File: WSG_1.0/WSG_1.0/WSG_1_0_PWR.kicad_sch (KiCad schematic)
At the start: 37 parts, among them J2 USB_C_Receptacle_USB2.0_16P, J4 Conn_01x02, U10 TPS22916CYFPR, U11 W25N04KVZEIR, U12 USBLC6-2SC6, U7 BQ25180YBGR, U8 TPS63802DLAR, U9 TPS7A2025PDBVR

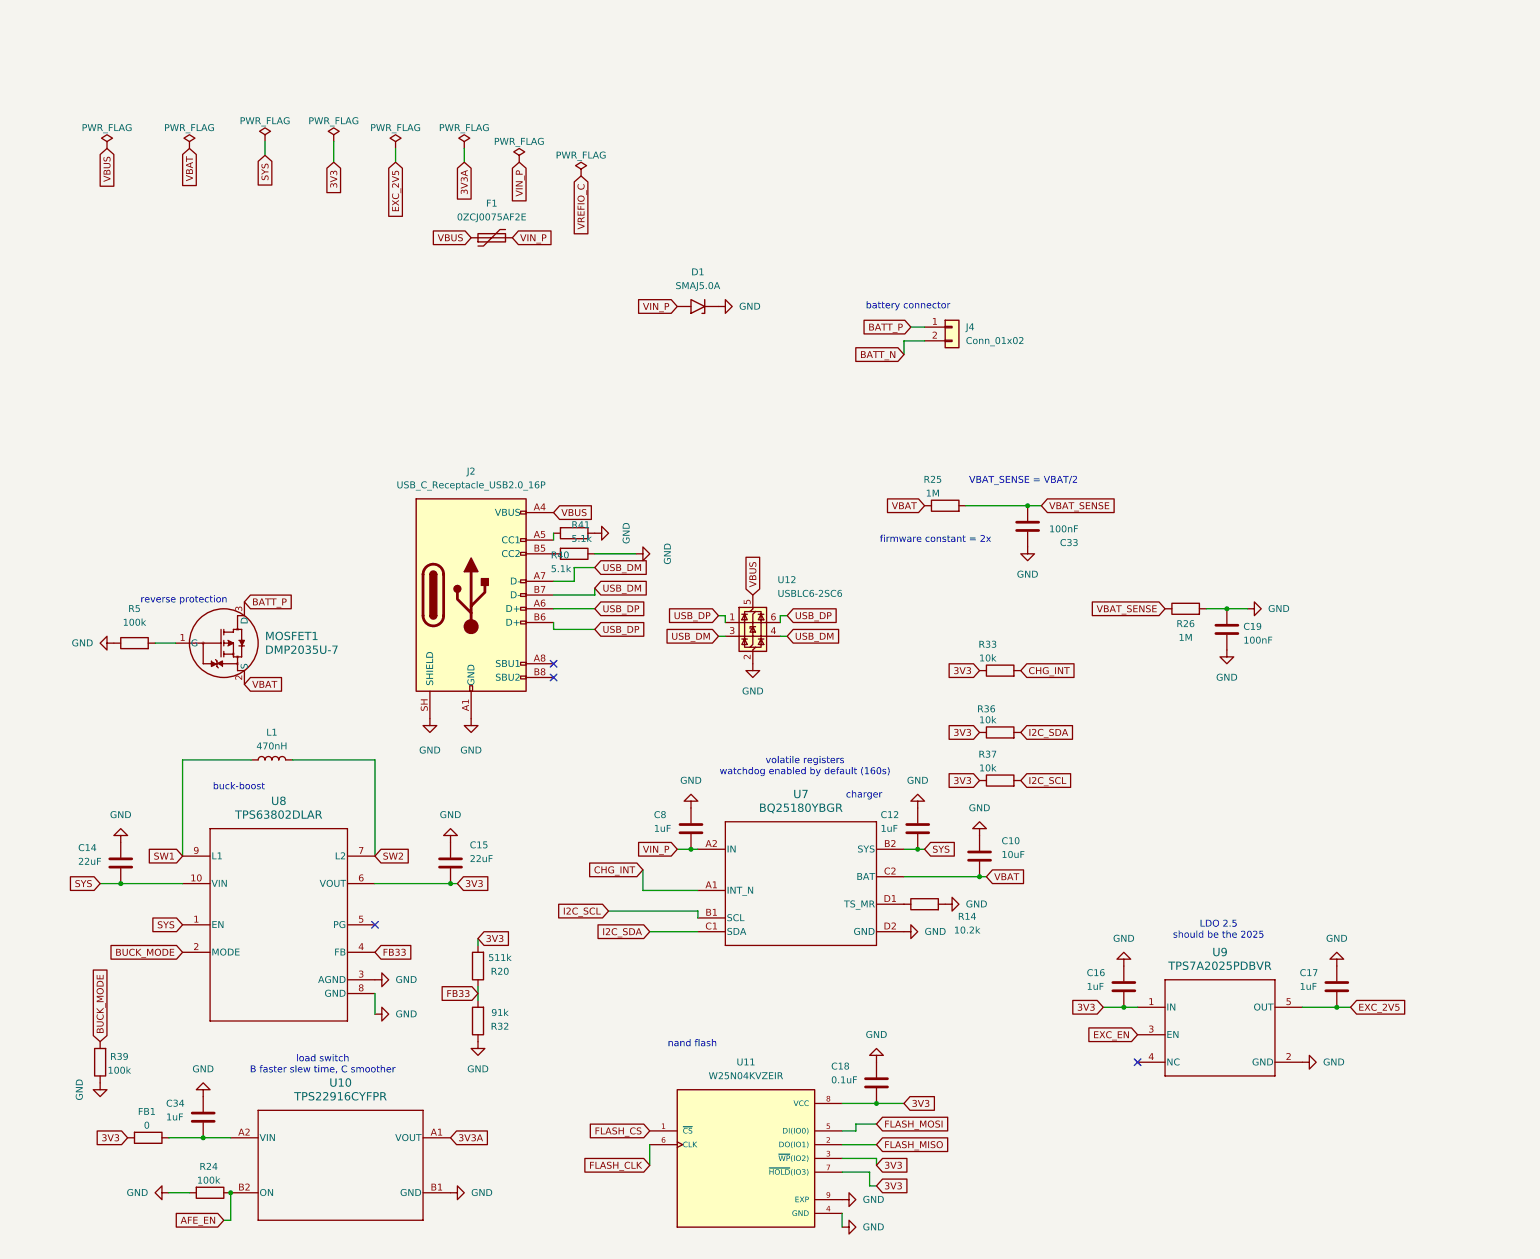
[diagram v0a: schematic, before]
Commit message: new layout started, clusters almost done
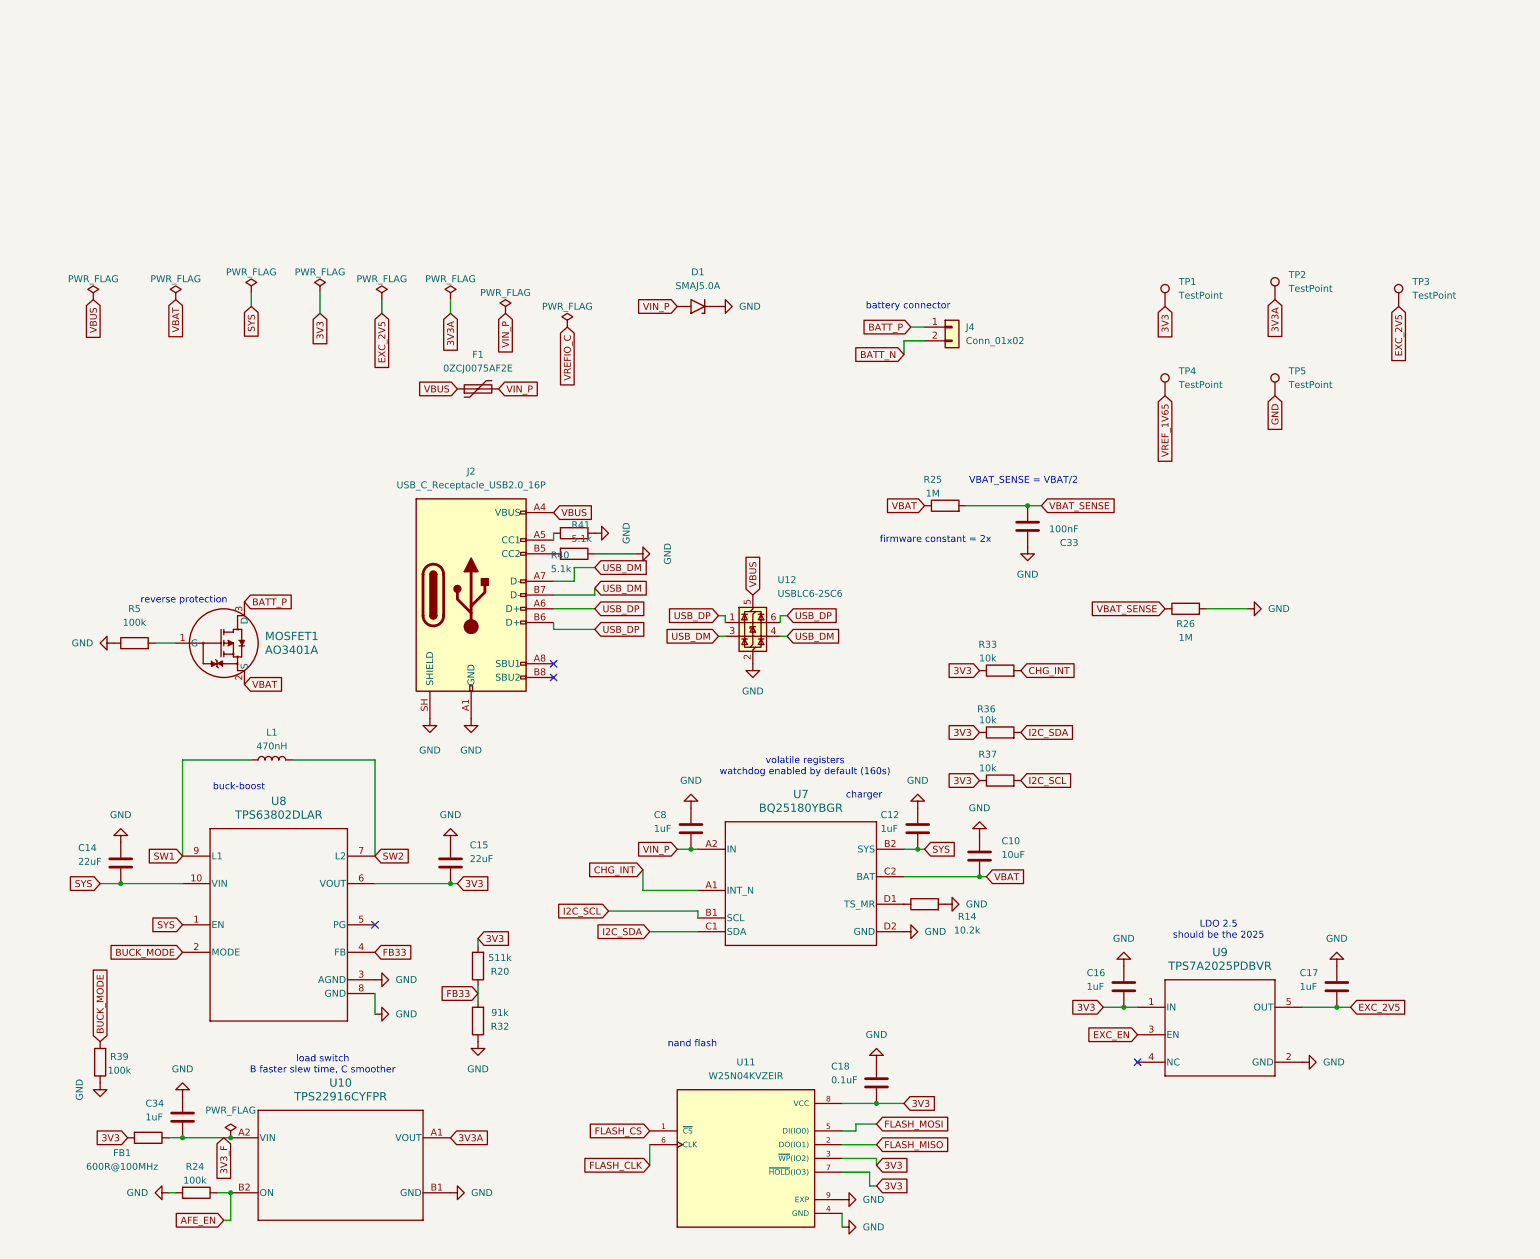
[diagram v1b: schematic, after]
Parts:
- removed C19: 100nF, Capacitor_SMD:C_0402_1005Metric_Pad0.74x0.62mm_HandSolder, symbol Device:C
- added TP1, TP2, TP3, TP4, TP5: TestPoint, TestPoint:TestPoint_Pad_1.0x1.0mm, symbol Connector:TestPoint
- FB1: value 0 -> 600R@100MHz; footprint Resistor_SMD:R_0402_1005Metric_Pad0.72x0.64mm_HandSolder -> Inductor_SMD:L_0402_1005Metric
- MOSFET1: value DMP2035U-7 -> AO3401A
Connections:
- net 3V3: now also TP1.1
- net 3V3A: now also TP2.1
- net EXC_2V5: now also TP3.1
- net GND: now also TP5.1
- net 3V3_F: now reaches C34.2, FB1.1, U10.A2 (VIN)
- new net VREF_1V65: TP4.1
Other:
- moved on the sheet: C34, F1, R24

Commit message: new layout, trying different layout onw
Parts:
- added C2: 1uF, Capacitor_SMD:C_0402_1005Metric_Pad0.74x0.62mm_HandSolder, symbol Device:C
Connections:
- net 3V3A: now also C2.2
- net GND: now also C2.1
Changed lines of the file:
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@@
 	)
 	(junction
+		(at 86.36 175.26)
+		(diameter 0)
+		(color 0 0 0 0)
+	)
+	(junction
 		(at 34.29 175.26)
 		(diameter 0)
@@
 	(wire
 		(pts
+			(xy 86.36 175.26) (xy 83.82 175.26)
+		)
+		(stroke
+			(width 0)
+			(type default)
+		)
+	)
+	(wire
+		(pts
 			(xy 69.85 148.59) (xy 69.85 152.4)
 		)
@@
 	(wire
 		(pts
+			(xy 91.44 175.26) (xy 86.36 175.26)
+		)
+		(stroke
+			(width 0)
+			(type default)
+		)
+	)
+	(wire
+		(pts
 			(xy 88.9 147.32) (xy 88.9 149.86)
 		)
@@
 	(global_label "3V3A"
 		(shape input)
-		(at 83.82 175.26 0)
+		(at 91.44 175.26 0)
 		(fields_autoplaced yes)
 		(effects
@@
 		)
 		(property "Intersheetrefs" "${INTERSHEET_REFS}"
-			(at 91.4014 175.26 0)
+			(at 99.0214 175.26 0)
 			(hide yes)
 			(show_name no)
@@
 	)
 	(symbol
+		(lib_id "power:GND")
+		(at 86.36 167.64 180)
+		(unit 1)
+		(body_style 1)
+		(exclude_from_sim no)
+		(in_bom yes)
+		(on_board yes)
+		(in_pos_files yes)
+		(dnp no)
+		(property "Reference" "#PWR066"
+			(at 86.36 161.29 0)
+			(hide yes)
+			(show_name no)
+			(do_not_autoplace no)
+			(effects
+				(font
+					(size 1.27 1.27)
+				)
+			)
+		)
+		(property "Value" "GND"
+			(at 83.312 166.37 0)
+			(show_name no)
+			(do_not_autoplace no)
+			(effects
+				(font
+					(size 1.27 1.27)
+				)
+			)
+		)
+		(property "Footprint" ""
+			(at 86.36 167.64 0)
+			(hide yes)
+			(show_name no)
+			(do_not_autoplace no)
+			(effects
+				(font
+					(size 1.27 1.27)
+				)
+			)
+		)
+		(property "Datasheet" ""
+			(at 86.36 167.64 0)
+			(hide yes)
+			(show_name no)
+			(do_not_autoplace no)
+			(effects
+				(font
+					(size 1.27 1.27)
+				)
+			)
+		)
+		(property "Description" "Power symbol creates a global label with name \"GND\" , ground"
+			(at 86.36 167.64 0)
+			(hide yes)
+			(show_name no)
+			(do_not_autoplace no)
+			(effects
+				(font
+					(size 1.27 1.27)
+				)
+			)
+		)
+		(pin "1"
+		)
+		(instances
+			(project "WSG_1.0"
+				(path "/cb65811d-b245-4002-a5a3-eef29f2c4ddb/05f78620-165f-4d12-a698-3b5ab7aa33dd"
+					(reference "#PWR066")
+					(unit 1)
+				)
+			)
+		)
+	)
+	(symbol
 		(lib_id "power:PWR_FLAG")
 		(at 17.78 20.32 0)
@@
 					(unit 1)
 				)
+			)
+		)
+	)
+	(symbol
+		(lib_id "Device:C")
+		(at 86.36 171.45 0)
+		(unit 1)
+		(body_style 1)
+		(exclude_from_sim no)
+		(in_bom yes)
+		(on_board yes)
+		(in_pos_files yes)
+		(dnp no)
+		(fields_autoplaced yes)
+		(property "Reference" "C2"
+			(at 90.17 170.1799 0)
+			(show_name no)
+			(do_not_autoplace no)
+			(effects
+				(font
+					(size 1.27 1.27)
+				)
+				(justify left)
+			)
+		)
+		(property "Value" "1uF"
+			(at 90.17 172.7199 0)
+			(show_name no)
+			(do_not_autoplace no)
+			(effects
+				(font
+					(size 1.27 1.27)
+				)
+				(justify left)
+			)
+		)
+		(property "Footprint" "Capacitor_SMD:C_0402_1005Metric_Pad0.74x0.62mm_HandSolder"
+			(at 87.3252 175.26 0)
+			(hide yes)
+			(show_name no)
+			(do_not_autoplace no)
+			(effects
+				(font
+					(size 1.27 1.27)
+				)
+			)
+		)
+		(property "Datasheet" ""
+			(at 86.36 171.45 0)
+			(hide yes)
+			(show_name no)
+			(do_not_autoplace no)
+			(effects
+				(font
+					(size 1.27 1.27)
+				)
+			)
+		)
+		(property "Description" "Unpolarized capacitor"
+			(at 86.36 171.45 0)
+			(hide yes)
+			(show_name no)
+			(do_not_autoplace no)
+			(effects
+				(font
+					(size 1.27 1.27)
+				)
+			)
+		)
+		(pin "2"
+		)
+		(pin "1"
+		)
+		(instances
+			(project "WSG_1.0"
+				(path "/cb65811d-b245-4002-a5a3-eef29f2c4ddb/05f78620-165f-4d12-a698-3b5ab7aa33dd"
+					(reference "C2")
+					(unit 1)
+				)

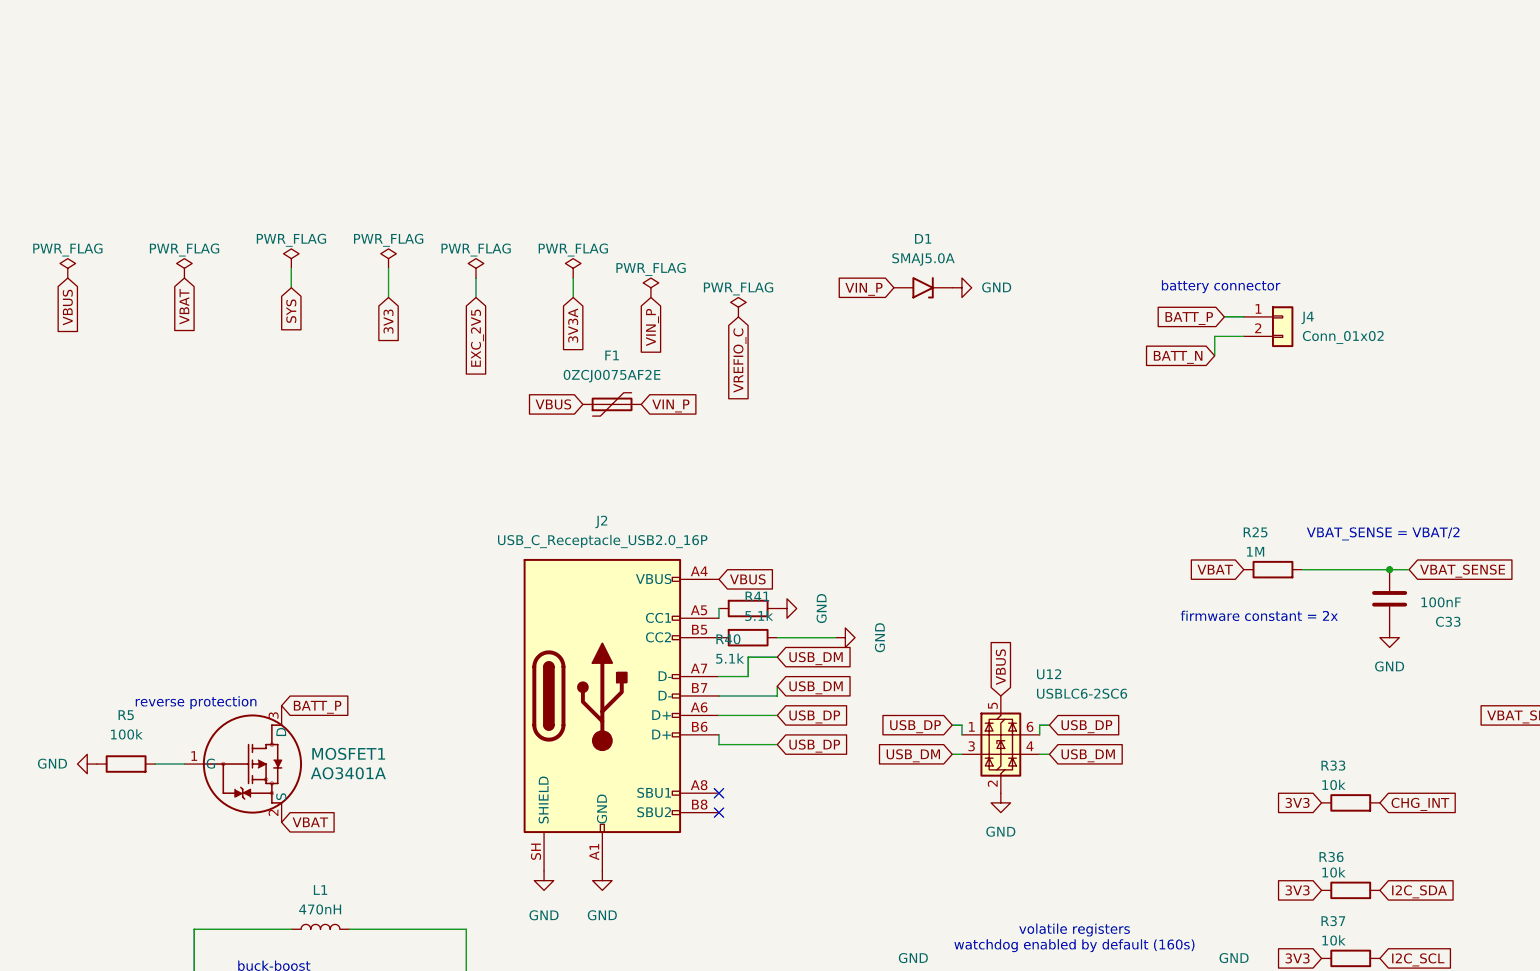
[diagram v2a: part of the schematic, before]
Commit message: adc schematic reforming
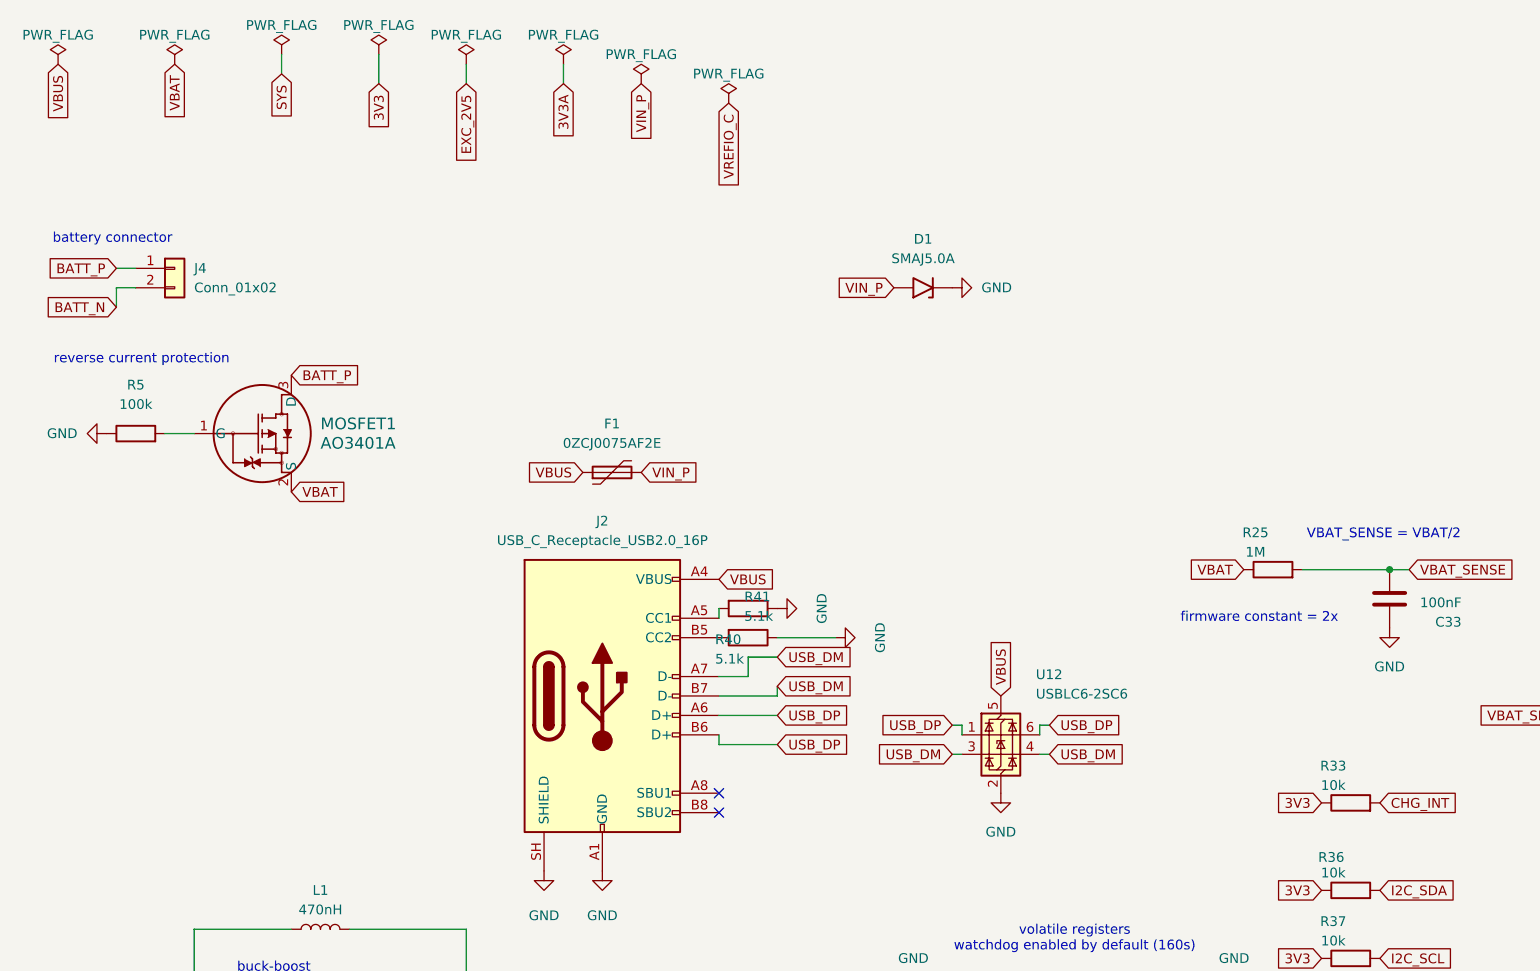
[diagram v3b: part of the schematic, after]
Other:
- note added: "reverse current protection"
- note removed: "reverse protection"
- moved on the sheet: F1, J4, MOSFET1, R5

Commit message: ~1/2 done with routing, neeed to undo some
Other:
- note added: "MEMS Oscillator"
- moved on the sheet: C16, C17, F1, J2, R40, R41, TP1, TP2, TP3, TP4, TP5, U12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
